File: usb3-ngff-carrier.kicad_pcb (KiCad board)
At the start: 4 copper layers, 90 x 40 mm, 62 parts, among them J1 KUSBX-BS1N9-1-BL30, J2 2199119-3, J3 Jack-DC, J4 SIM8060-6-1-14-00-A, J5 Conn_01x03_Male, J6 SIM8060-6-1-14-00-A, SW1 KMR221GLFS, U1 AP62301WU7

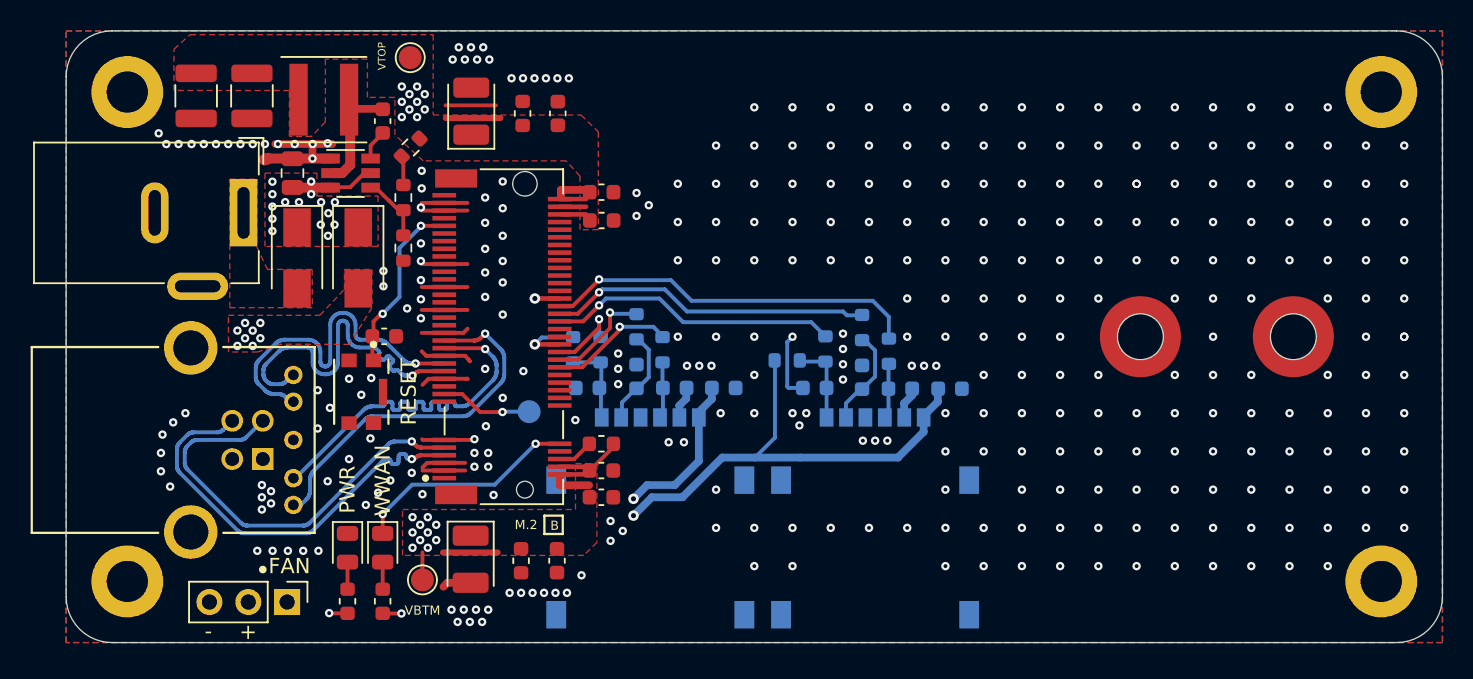
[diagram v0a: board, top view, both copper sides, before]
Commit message: feat: changes sim card holder to 2FF and adds missing PN to resistors
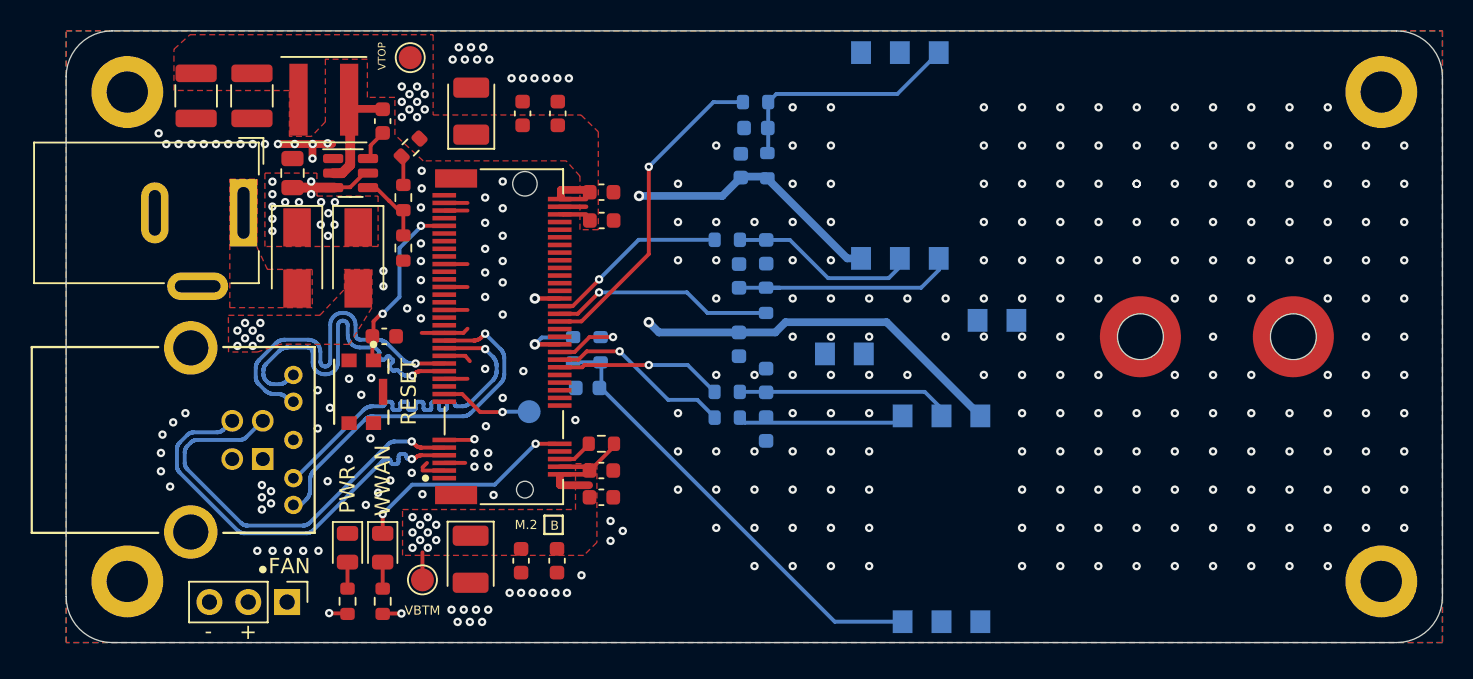
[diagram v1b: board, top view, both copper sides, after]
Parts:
- removed J4: SIM8060-6-1-14-00-A, footprint:GCT_SIM8060-6-1-14-00-A
- added J8: SIM2070-6-1-30-00-A, SamacSys_Parts:SIM2070613000A_card, B.Cu at (55.9, 29.9)
- J6: value SIM8060-6-1-14-00-A -> SIM2070-6-1-30-00-A; footprint footprint:GCT_SIM8060-6-1-14-00-A -> SamacSys_Parts:SIM2070613000A_card
- moved J6 22.1 mm to (55.9, 10.2), turned to 90 degrees
- moved C16 20.0 mm to (44.1, 8.81), turned to 90 degrees
- moved C19 17.4 mm to (45.1, 6.35)
- moved R8 16.8 mm to (45.1, 4.66), turned to 180 degrees
- moved R6 12.8 mm to (43.2, 13.7), turned to 180 degrees
- moved R14 12.8 mm to (45.9, 8.81), turned to 90 degrees
- moved C17 12.5 mm to (45.8, 14.4), turned to -90 degrees
- moved C18 10.4 mm to (44.0, 16.0)
- moved C22 9.14 mm to (45.8, 26.0), turned to -90 degrees
- moved R11 8.40 mm to (43.2, 25.3), turned to 180 degrees
- moved R7 6.53 mm to (45.8, 17.6), turned to -90 degrees
- moved C21 5.99 mm to (45.8, 22.9), turned to 90 degrees
- moved R10 5.05 mm to (43.2, 23.6), turned to 180 degrees
- moved C20 3.02 mm to (44.0, 20.5), turned to -90 degrees
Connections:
- J2 pad 1: Net-(J2-Pad1) -> unconnected-(J2-Pad1)
- J2 pad 20: Net-(J2-Pad20) -> unconnected-(J2-Pad20)
- J2 pad 21: Net-(J2-Pad21) -> unconnected-(J2-Pad21)
- J2 pad 22: Net-(J2-Pad22) -> unconnected-(J2-Pad22)
- J2 pad 24: Net-(J2-Pad24) -> unconnected-(J2-Pad24)
- J2 pad 25: Net-(J2-Pad25) -> unconnected-(J2-Pad25)
- J2 pad 26: Net-(J2-Pad26) -> unconnected-(J2-Pad26)
- J2 pad 28: Net-(J2-Pad28) -> unconnected-(J2-Pad28)
- J2 pad 38: Net-(J2-Pad38) -> unconnected-(J2-Pad38)
- J2 pad 40: Net-(J2-Pad40) -> unconnected-(J2-Pad40)
- J2 pad 41: Net-(J2-Pad41) -> unconnected-(J2-Pad41)
- J2 pad 43: Net-(J2-Pad43) -> unconnected-(J2-Pad43)
- J2 pad 47: Net-(J2-Pad47) -> unconnected-(J2-Pad47)
- J2 pad 49: Net-(J2-Pad49) -> unconnected-(J2-Pad49)
- J2 pad 50: Net-(J2-Pad50) -> unconnected-(J2-Pad50)
- J2 pad 52: Net-(J2-Pad52) -> unconnected-(J2-Pad52)
- J2 pad 53: Net-(J2-Pad53) -> unconnected-(J2-Pad53)
- J2 pad 54: Net-(J2-Pad54) -> unconnected-(J2-Pad54)
- J2 pad 55: Net-(J2-Pad55) -> unconnected-(J2-Pad55)
- J2 pad 56: Net-(J2-Pad56) -> unconnected-(J2-Pad56)
- J2 pad 58: Net-(J2-Pad58) -> unconnected-(J2-Pad58)
- J2 pad 59: Net-(J2-Pad59) -> unconnected-(J2-Pad59)
- J2 pad 60: Net-(J2-Pad60) -> unconnected-(J2-Pad60)
- J2 pad 61: Net-(J2-Pad61) -> unconnected-(J2-Pad61)
- J2 pad 62: Net-(J2-Pad62) -> unconnected-(J2-Pad62)
- J2 pad 63: Net-(J2-Pad63) -> unconnected-(J2-Pad63)
- J2 pad 64: Net-(J2-Pad64) -> unconnected-(J2-Pad64)
- J2 pad 66: Net-(J2-Pad66) -> unconnected-(J2-Pad66)
- J2 pad 68: Net-(J2-Pad68) -> unconnected-(J2-Pad68)
- J2 pad 69: Net-(J2-Pad69) -> unconnected-(J2-Pad69)
- J2 pad 75: Net-(J2-Pad75) -> unconnected-(J2-Pad75)
- J2 pad 8: Net-(J2-Pad8) -> unconnected-(J2-Pad8)
- J3 pad 3: (no net) -> GND
- J5 pad 1: Net-(J5-Pad1) -> unconnected-(J5-Pad1)
- J6 pad C6: Net-(J6-PadC6) -> unconnected-(J6-PadC6)
- SW1 pad 2: Net-(SW1-Pad2) -> unconnected-(SW1-Pad2)
- SW1 pad 3: Net-(SW1-Pad3) -> unconnected-(SW1-Pad3)
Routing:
- net GND: track 56.3 -> 23.5 mm, vias 337 -> 304
- net Net-(J8-PadC7): track 4.77 -> 29.3 mm
- net /USIM2_VDD: track 50.6 -> 28.4 mm
- net /USIM2_RST: track 24.7 -> 11.9 mm
- net Net-(C21-Pad1): track 2.75 -> 14.1 mm
- net Net-(C19-Pad1): track 4.72 -> 15.8 mm
- net /USIM1_VDD: track 27.5 -> 37.1 mm
- net Net-(C18-Pad1): track 5.83 -> 15.3 mm
- net Net-(C17-Pad1): track 3.25 -> 12.4 mm
- net +3V8: track 27.4 -> 20.0 mm
- net /USIM2_CLK: track 21.2 -> 14.6 mm
- net Net-(C22-Pad1): track 5.81 -> 11.2 mm
- net /USIM1_CLK: track 6.94 -> 12.2 mm
- net /USIM1_RST: track 8.21 -> 10.9 mm
- net /USIM2_DATA: track 18.4 -> 20.7 mm
- added copper zone on In1.Cu, net +3V8
- added copper zone on In2.Cu, net GND
- added copper zone on In1.Cu, net VBUS
- added copper zone on In1.Cu, net VSYS
- removed copper zone on In1.CuPwr, net +3V8
- removed copper zone on In2.CuGnd, net GND
- removed copper zone on In1.CuPwr, net VBUS
- removed copper zone on In1.CuPwr, net VSYS
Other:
- net class Default removed
- net class DiffPairs removed
- board text added: "SIM 1"
- board text added: "SIM 2"
- board text removed: "JLCJLCJLCJLC"
- board text removed: "USIM 1"
- board text removed: "USIM 2"
